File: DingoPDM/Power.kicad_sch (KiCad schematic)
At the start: 14 parts, among them U1 VXO780x-500-M, U2 LD1117S33CTR

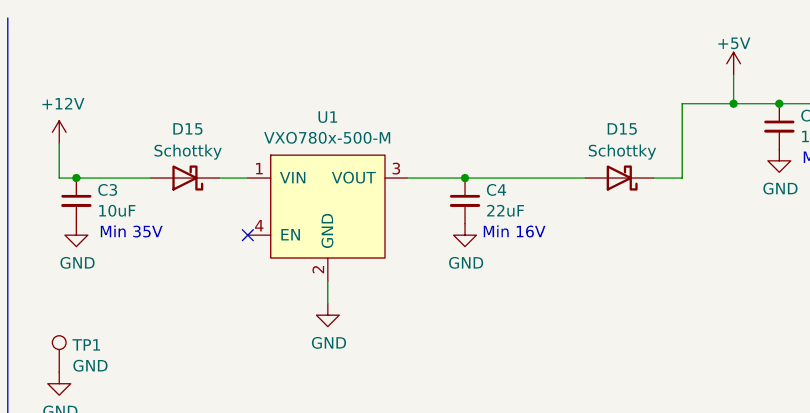
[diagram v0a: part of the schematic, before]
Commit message: Updated to Kicad 8
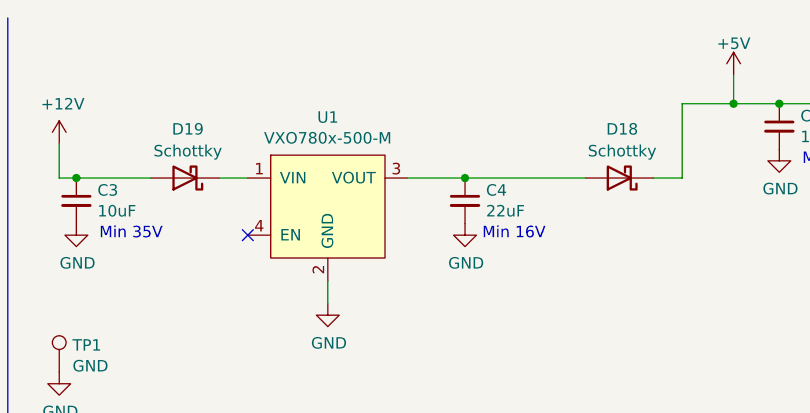
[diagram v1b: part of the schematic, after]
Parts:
- renumbered D15 to D18, D15 to D19

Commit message: add DC-DC converter options
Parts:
- added U14: OKI-78SR-5_1.5-W36H-C, Converter_DCDC:Converter_DCDC_Murata_OKI-78SR_Horizontal, symbol Converter_DCDC:OKI-78SR-5_1.5-W36H-C
- added U15: TSR_1-2450, Converter_DCDC:Converter_DCDC_TRACO_TSR-1_THT, symbol Regulator_Switching:TSR_1-2450
- U1: value VXO780x-500-M -> VXO7805-500-M
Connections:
- net GND: now also U14.2 (GND), U15.2 (GND)
- net +12P: now reaches D19.1 (K), U1.1 (VIN)
- net +12P: now also U14.1 (IN), U15.1 (Vin)
- net +5VP: now reaches C4.1, D18.2 (A), U1.3 (VOUT)
- net +5VP: now also U14.3 (OUT), U15.3 (Vout)
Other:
- note added: "DC-DC Options"
- note added: "U1 Options: CUI VXO7805-500-M-TR (6.5V-36V) Recom ROF-78E5.0-0.5SMD-R (9V-36V) U1 Thru-Hole Option: Traco Power TSR 1-2450 (6.5V-36V) Murata OKI-78SR-5_1.5-W36H-C (7V-36V) Note: 10mm max height PCB to case"
- note added: "Use one in place of U1"
- title: Dingo_PDM -> dingoPDM

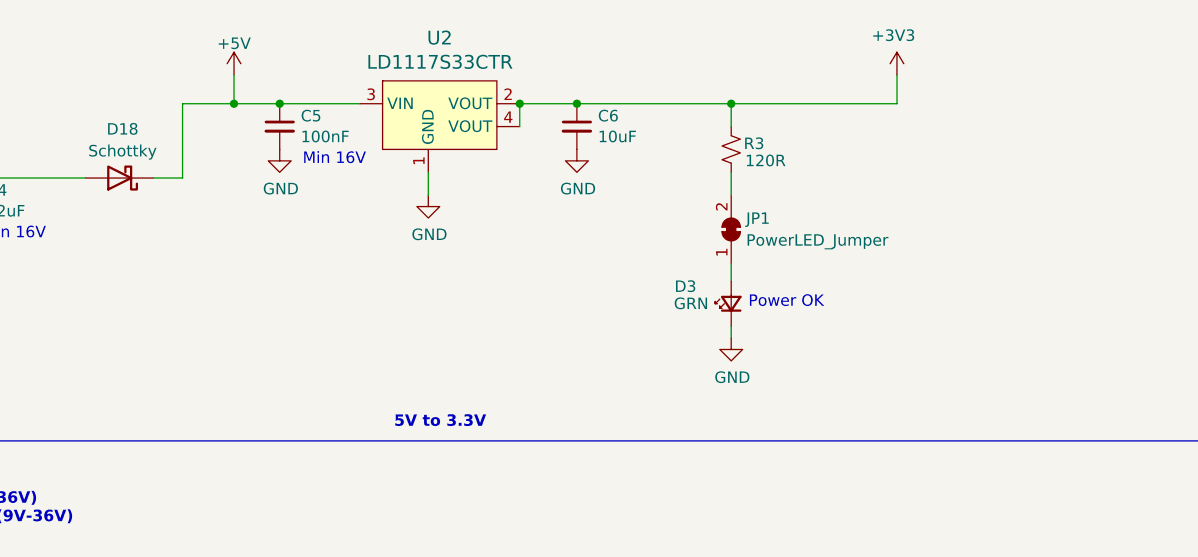
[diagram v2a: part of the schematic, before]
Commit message: add 5v cap
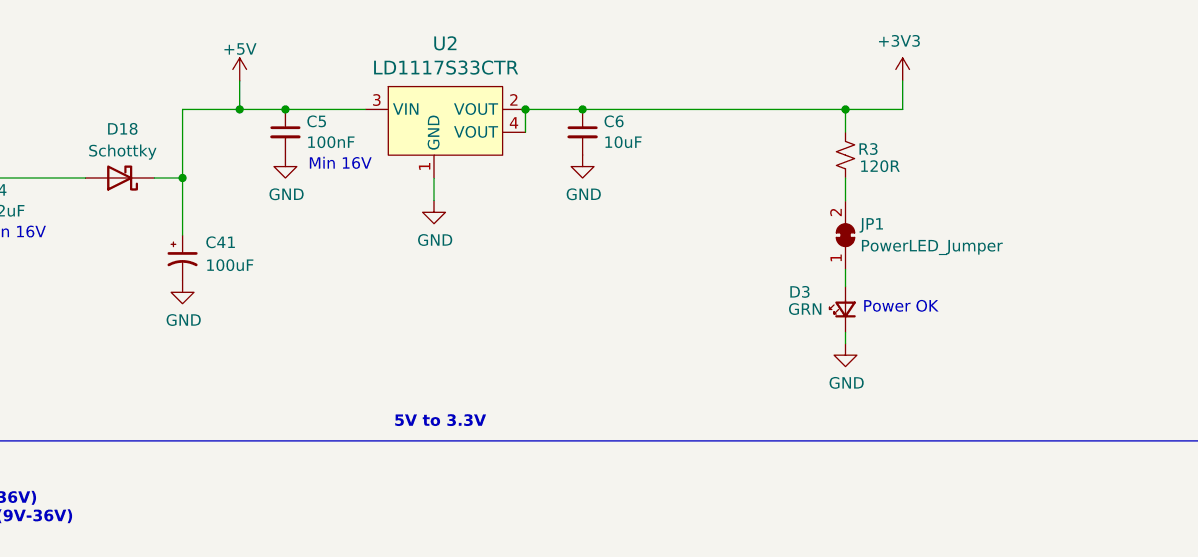
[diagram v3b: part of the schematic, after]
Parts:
- added C41: 100uF, Capacitor_SMD:C_Elec_6.3x7.7, symbol Device:C_Polarized_Small_US
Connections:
- net +5V: now also C41.1
- net GND: now also C41.2
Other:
- moved on the sheet: C5, C6, D3, JP1, R3, U2
